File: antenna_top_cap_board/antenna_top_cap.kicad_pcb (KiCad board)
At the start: 4 copper layers, 100 x 100 mm, 57 parts, among them IC1 PCT2075DP,118, J1 Battery Charge Bypass, J10 USB_B_Micro, J11 USB_B_Micro, J13 USB_B_Micro, J14 BM04B-SRSS-TB(LF)(SN), J15 USB_B_Micro, J16 BM04B-SRSS-TB(LF)(SN), J17 BM04B-SRSS-TB(LF)(SN), J18 BM04B-SRSS-TB(LF)(SN)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

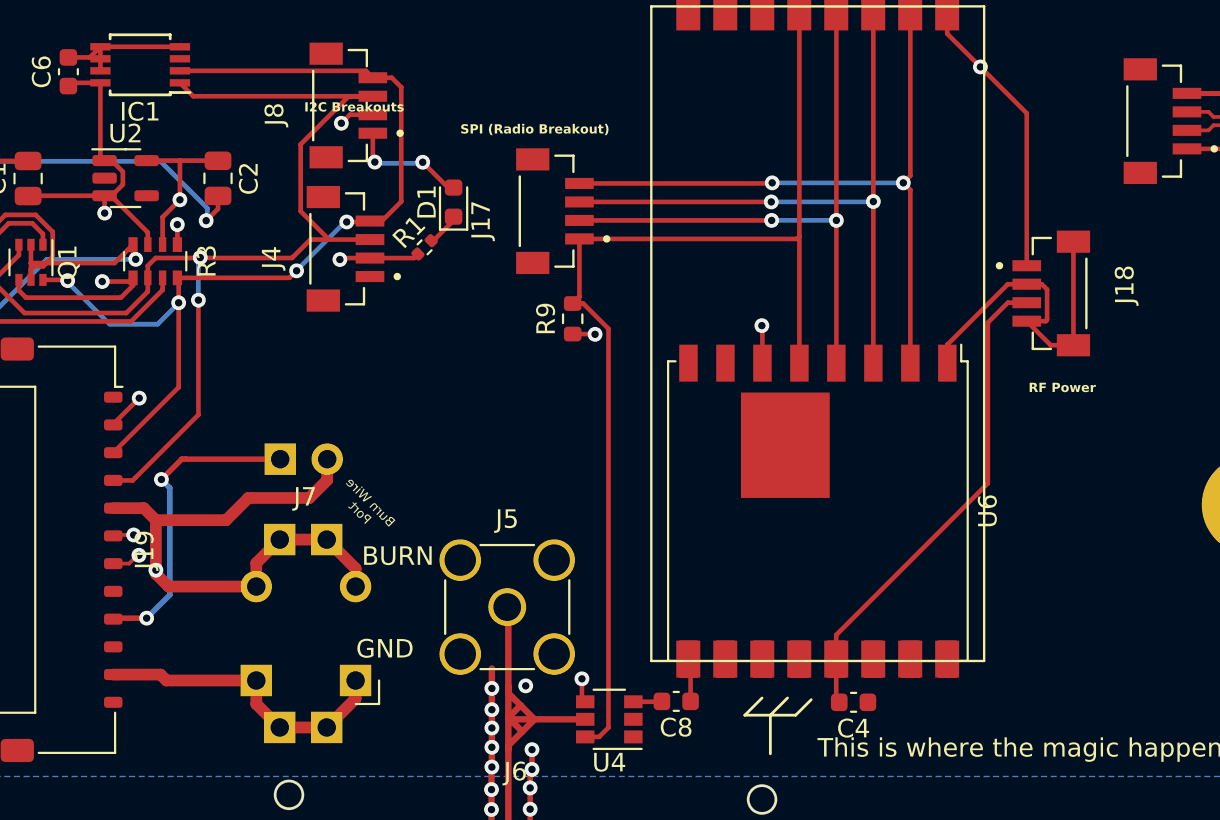
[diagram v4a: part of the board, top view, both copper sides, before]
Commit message: Finished Connecting 12Pos Connections
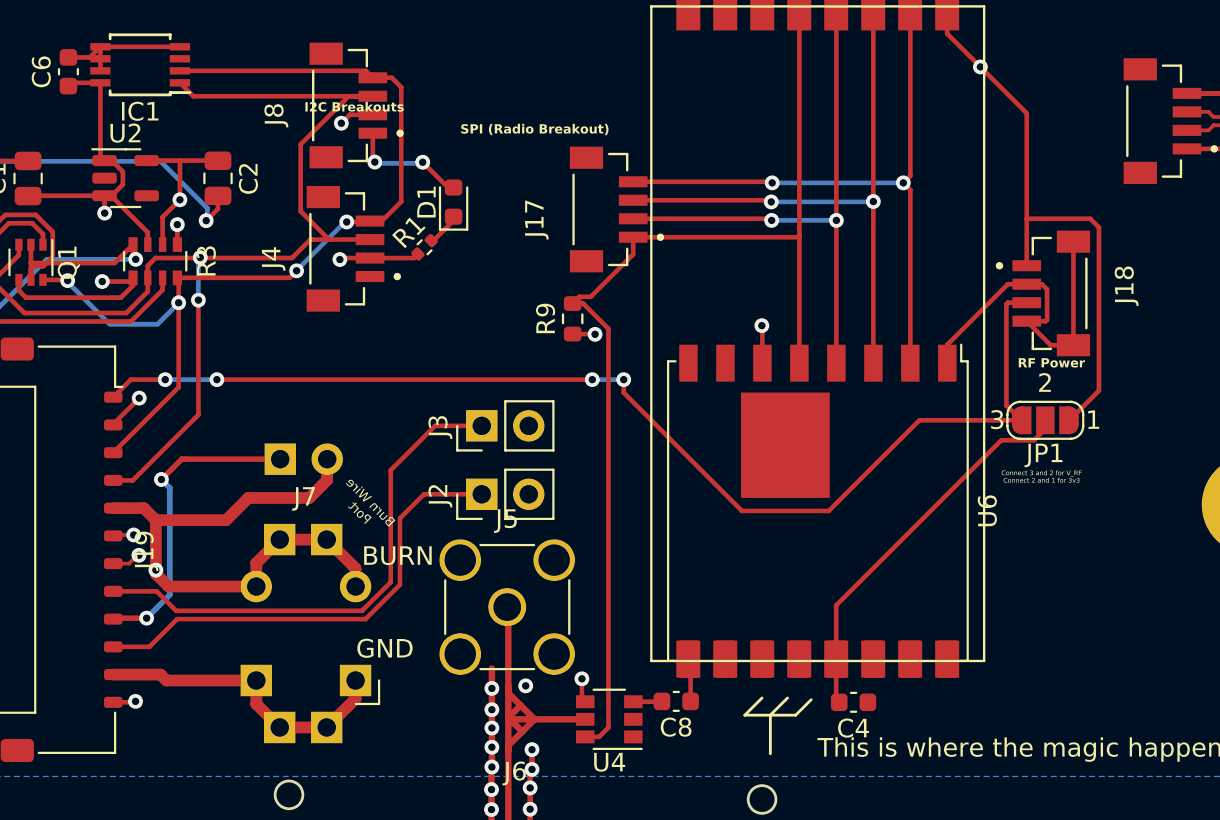
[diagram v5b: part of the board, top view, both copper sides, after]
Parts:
- added J2: Conn_01x02, Connector_PinHeader_2.54mm:PinHeader_1x02_P2.54mm_Vertical, F.Cu at (163.2, 111.6)
- added J3: Conn_01x02, Connector_PinHeader_2.54mm:PinHeader_1x02_P2.54mm_Vertical, F.Cu at (163.2, 107.9)
- added JP1: SolderJumper_3_Open, Jumper:SolderJumper-3_P1.3mm_Open_RoundedPad1.0x1.5mm_NumberLabels, F.Cu at (193.6, 107.6)
- moved J17 2.91 mm to (168.8, 96.2)
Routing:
- net V_RF: track 0.00 -> 62.6 mm, vias 0 -> 4
- net ~{RESET}: track 0.00 -> 28.1 mm
- net USBBOOT: track 0.00 -> 25.4 mm
- net 3.3V: track 47.6 -> 62.8 mm
- net RF_VCC: track 26.5 -> 21.0 mm
- net SPI0_MOSI: track 34.9 -> 32.0 mm
- net SPI0_SCK: track 32.9 -> 30.0 mm
- net SPI0_MISO: track 36.8 -> 34.0 mm
- net SPI0_CS0: track 60.1 -> 58.8 mm
- net GND: track 192.6 -> 193.8 mm, vias 31 -> 32
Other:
- board text added: "Connect 3 and 2 for V_RF Connect 2 and 1 for 3v3"

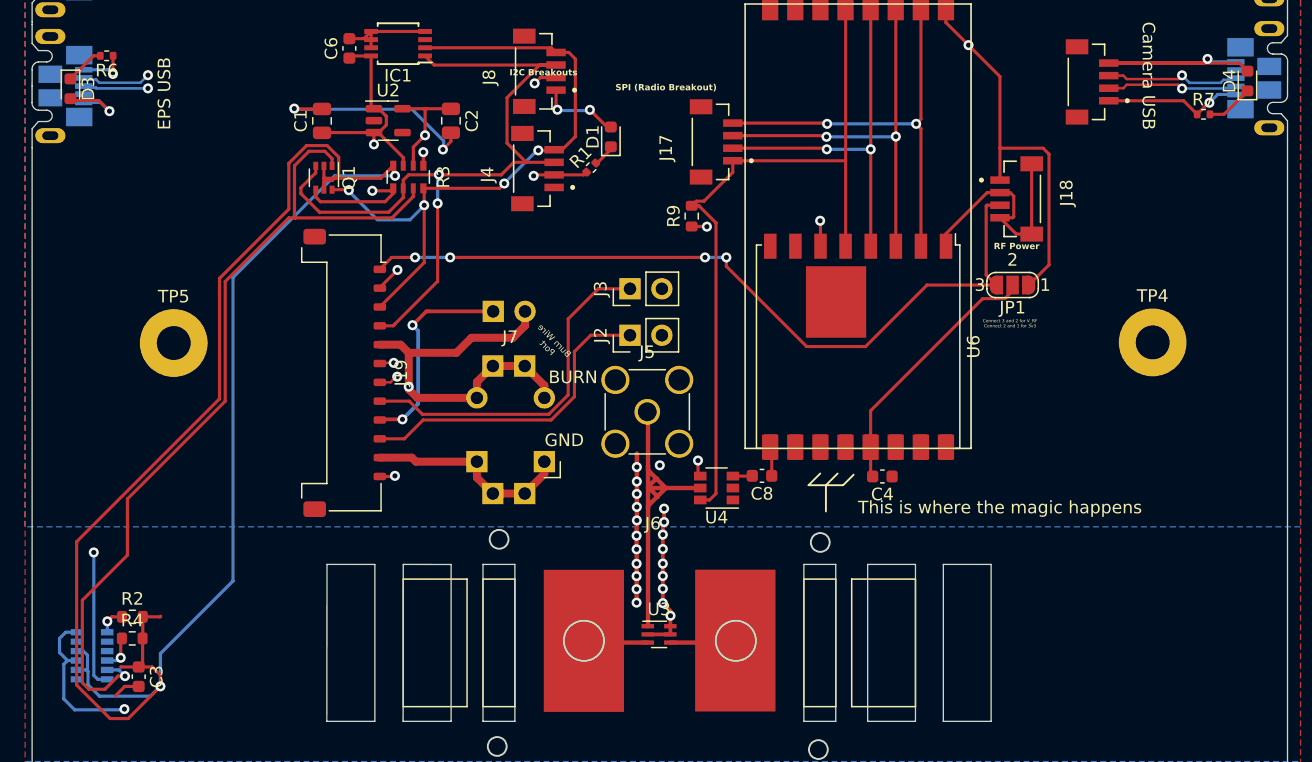
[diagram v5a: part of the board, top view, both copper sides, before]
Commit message: Addressed all DRC Errors
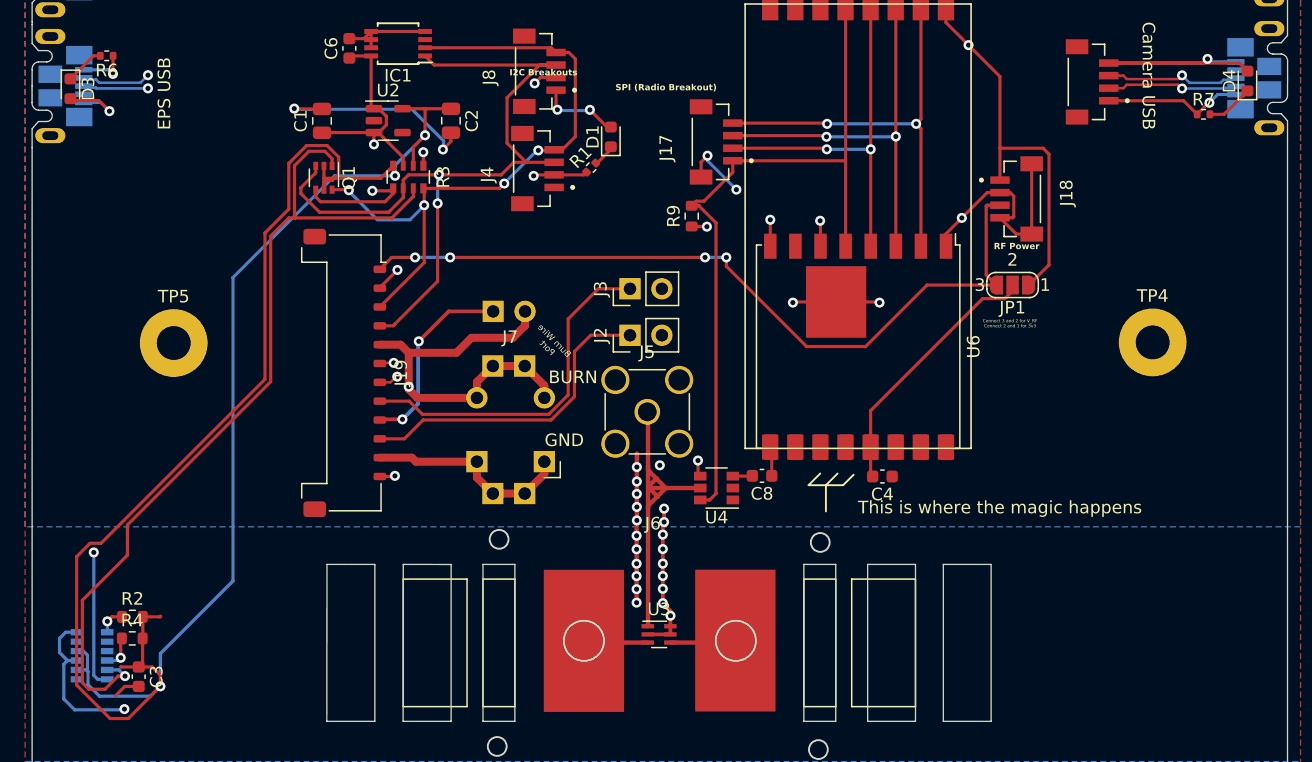
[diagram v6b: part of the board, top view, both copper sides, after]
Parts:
- added G***: LOGO, LOGO, B.Cu at (159.5, 124.0)
- moved G*** 3.28 mm to (159.5, 124.0)
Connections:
- J4 pad S1: Net-(J4-SHIELD-PadS1) -> unconnected-(J4-SHIELD-PadS1)_0
- J4 pad S2: Net-(J4-SHIELD-PadS1) -> unconnected-(J4-SHIELD-PadS1)
- J8 pad S1: Net-(J8-SHIELD-PadS1) -> unconnected-(J8-SHIELD-PadS1)_0
- J8 pad S2: Net-(J8-SHIELD-PadS1) -> unconnected-(J8-SHIELD-PadS1)
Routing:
- net GND: track 193.8 -> 208.4 mm, vias 32 -> 38
- net 2.8V: track 155.1 -> 159.7 mm
- net Dir_Chrg_In: track 16.9 -> 15.5 mm
